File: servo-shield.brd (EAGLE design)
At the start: 65 x 56 mm, 30 parts, among them IC1 24AA01P, K1 PIN20X2

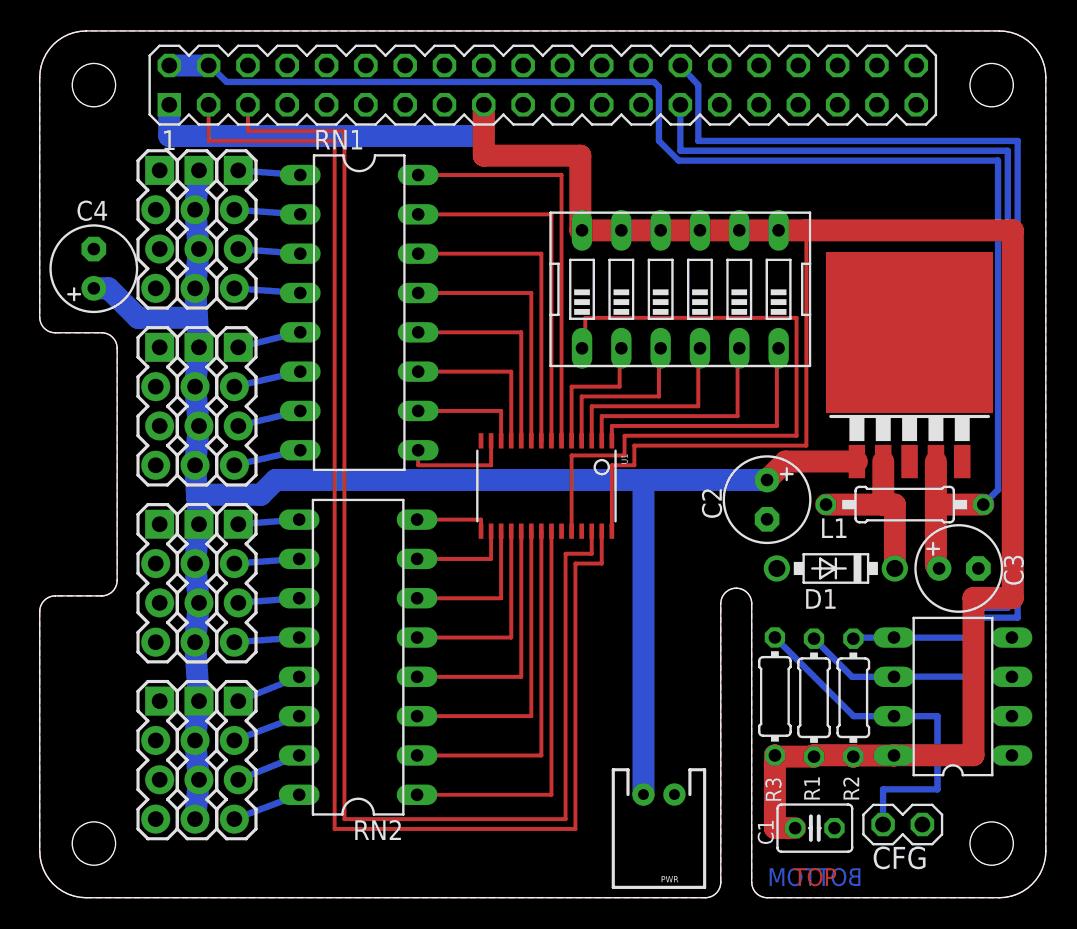
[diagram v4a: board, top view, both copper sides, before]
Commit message: Fix DRC errors. Wish I'd done that before ordering the blasted boards
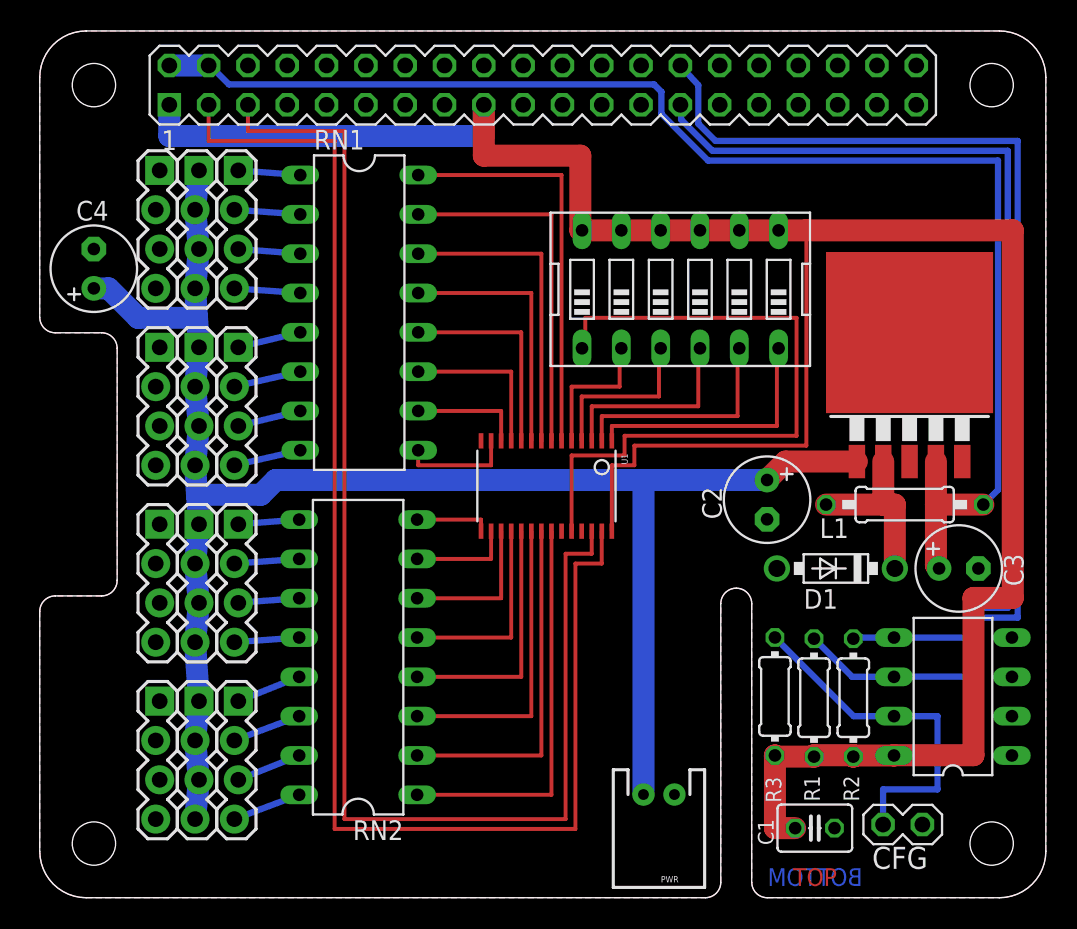
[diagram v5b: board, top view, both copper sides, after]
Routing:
- net ID_SDA: track 65.6 -> 64.4 mm
- net +5V: track 90.8 -> 89.6 mm
- net ID_SCL: track 74.8 -> 74.1 mm
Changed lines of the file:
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@@
 <?xml version="1.0" encoding="utf-8"?>
 <!DOCTYPE eagle SYSTEM "eagle.dtd">
-<eagle version="6.5.0">
+<eagle version="7.0.0">
 <drawing>
 <settings>
@@
 <setting verticaltext="up"/>
 </settings>
-<grid distance="0.0125" unitdist="inch" unit="inch" style="lines" multiple="1" display="yes" altdistance="0.025" altunitdist="inch" altunit="inch"/>
+<grid distance="0.00625" unitdist="inch" unit="inch" style="dots" multiple="1" display="yes" altdistance="0.025" altunitdist="inch" altunit="inch"/>
 <layers>
 <layer number="1" name="Top" color="4" fill="1" visible="yes" active="yes"/>
@@
 </class>
 </classes>
-<designrules name="ITEADstudio_DRC">
+<designrules name="LaenPCBOrder">
 <description language="de">&lt;b&gt;EAGLE Design Rules&lt;/b&gt;
 &lt;p&gt;
@@
 Einstellungen hier und speichern die Design Rules unter
 einem neuen Namen ab.</description>
-<description language="en">&lt;b&gt;EAGLE Design Rules&lt;/b&gt;
+<description language="en">&lt;b&gt;Laen's PCB Order Design Rules&lt;/b&gt;
 &lt;p&gt;
-The default Design Rules have been set to cover
-a wide range of applications. Your particular design
-may have different requirements, so please make the
-necessary adjustments and save your customized
-design rules under a new name.</description>
-<description language="zh">&lt;b&gt;Seeed Studio EAGLE Design Rules&lt;/b&gt;
-</description>
+Please make sure your boards conform to these design rules.</description>
 <param name="layerSetup" value="(1*16)"/>
-<param name="mtCopper" value="0.035mm 0.035mm 0.035mm 0.035mm 0.035mm 0.035mm 0.035mm 0.035mm 0.035mm 0.035mm 0.035mm 0.035mm 0.035mm 0.035mm 0.035mm 0.035mm"/>
-<param name="mtIsolate" value="1.5mm 0.15mm 0.2mm 0.15mm 0.2mm 0.15mm 0.2mm 0.15mm 0.2mm 0.15mm 0.2mm 0.15mm 0.2mm 0.15mm 0.2mm"/>
+<param name="mtCopper" value="0.0356mm 0.0356mm 0.0356mm 0.0356mm 0.0356mm 0.0356mm 0.0356mm 0.0356mm 0.0356mm 0.0356mm 0.0356mm 0.0356mm 0.0356mm 0.0356mm 0.0356mm 0.0356mm"/>
+<param name="mtIsolate" value="1.5011mm 0.1499mm 0.2007mm 0.1499mm 0.2007mm 0.1499mm 0.2007mm 0.1499mm 0.2007mm 0.1499mm 0.2007mm 0.1499mm 0.2007mm 0.1499mm 0.2007mm"/>
 <param name="mdWireWire" value="6mil"/>
 <param name="mdWirePad" value="6mil"/>
@@
 <param name="mdPadVia" value="6mil"/>
 <param name="mdViaVia" value="6mil"/>
-<param name="mdSmdPad" value="0mil"/>
-<param name="mdSmdVia" value="0mil"/>
-<param name="mdSmdSmd" value="0mil"/>
+<param name="mdSmdPad" value="6mil"/>
+<param name="mdSmdVia" value="6mil"/>
+<param name="mdSmdSmd" value="6mil"/>
 <param name="mdViaViaSameLayer" value="8mil"/>
 <param name="mnLayersViaInSmd" value="2"/>
-<param name="mdCopperDimension" value="10mil"/>
-<param name="mdDrill" value="10mil"/>
+<param name="mdCopperDimension" value="15mil"/>
+<param name="mdDrill" value="6mil"/>
 <param name="mdSmdStop" value="0mil"/>
 <param name="msWidth" value="6mil"/>
-<param name="msDrill" value="12mil"/>
-<param name="msMicroVia" value="12mil"/>
+<param name="msDrill" value="13mil"/>
+<param name="msMicroVia" value="13mil"/>
 <param name="msBlindViaRatio" value="0.5"/>
 <param name="rvPadTop" value="0.25"/>
@@
 <param name="rvMicroViaOuter" value="0.25"/>
 <param name="rvMicroViaInner" value="0.25"/>
-<param name="rlMinPadTop" value="10mil"/>
+<param name="rlMinPadTop" value="7mil"/>
 <param name="rlMaxPadTop" value="20mil"/>
-<param name="rlMinPadInner" value="10mil"/>
+<param name="rlMinPadInner" value="7mil"/>
 <param name="rlMaxPadInner" value="20mil"/>
-<param name="rlMinPadBottom" value="10mil"/>
+<param name="rlMinPadBottom" value="7mil"/>
 <param name="rlMaxPadBottom" value="20mil"/>
-<param name="rlMinViaOuter" value="6mil"/>
+<param name="rlMinViaOuter" value="7mil"/>
 <param name="rlMaxViaOuter" value="20mil"/>
-<param name="rlMinViaInner" value="6mil"/>
+<param name="rlMinViaInner" value="7mil"/>
 <param name="rlMaxViaInner" value="20mil"/>
 <param name="rlMinMicroViaOuter" value="4mil"/>
@@
 <param name="psTop" value="-1"/>
 <param name="psBottom" value="-1"/>
-<param name="psFirst" value="0"/>
+<param name="psFirst" value="-1"/>
 <param name="psElongationLong" value="100"/>
 <param name="psElongationOffset" value="100"/>
 <param name="mvStopFrame" value="1"/>
 <param name="mvCreamFrame" value="0"/>
-<param name="mlMinStopFrame" value="2mil"/>
-<param name="mlMaxStopFrame" value="2mil"/>
+<param name="mlMinStopFrame" value="3mil"/>
+<param name="mlMaxStopFrame" value="3mil"/>
 <param name="mlMinCreamFrame" value="0mil"/>
 <param name="mlMaxCreamFrame" value="0mil"/>
-<param name="mlViaStopLimit" value="100mil"/>
+<param name="mlViaStopLimit" value="0mil"/>
 <param name="srRoundness" value="0"/>
 <param name="srMinRoundness" value="0mil"/>
@@
 <param name="checkAngle" value="0"/>
 <param name="checkFont" value="1"/>
-<param name="checkRestrict" value="0"/>
+<param name="checkRestrict" value="1"/>
 <param name="useDiameter" value="13"/>
 <param name="maxErrors" value="50"/>
@@
 <pass name="Default">
 <param name="RoutingGrid" value="50mil"/>
+<param name="AutoGrid" value="1"/>
+<param name="Efforts" value="0"/>
+<param name="TopRouterVariant" value="1"/>
 <param name="tpViaShape" value="round"/>
 <param name="PrefDir.1" value="|"/>
@@
 <wire x1="57.8993" y1="21.4757" x2="58.1025" y2="21.2725" width="1.4224" layer="1"/>
 <wire x1="10.91" y1="53.77" x2="11" y2="53.77" width="0.4064" layer="16"/>
-<wire x1="11" y1="53.77" x2="12.065" y2="52.705" width="0.4064" layer="16"/>
-<wire x1="12.065" y1="52.705" x2="39.6875" y2="52.705" width="0.4064" layer="16"/>
-<wire x1="39.6875" y1="52.705" x2="40.005" y2="52.3875" width="0.4064" layer="16"/>
-<wire x1="40.005" y1="52.3875" x2="40.005" y2="48.895" width="0.4064" layer="16"/>
-<wire x1="40.005" y1="48.895" x2="41.275" y2="47.625" width="0.4064" layer="16"/>
-<wire x1="41.275" y1="47.625" x2="61.9125" y2="47.625" width="0.4064" layer="16"/>
+<wire x1="11" y1="53.77" x2="12.22375" y2="52.54625" width="0.4064" layer="16"/>
+<wire x1="12.22375" y1="52.54625" x2="39.6875" y2="52.54625" width="0.4064" layer="16"/>
+<wire x1="39.6875" y1="52.54625" x2="40.16375" y2="52.07" width="0.4064" layer="16"/>
+<wire x1="40.16375" y1="52.07" x2="40.16375" y2="50.64125" width="0.4064" layer="16"/>
+<wire x1="40.16375" y1="50.64125" x2="43.18" y2="47.625" width="0.4064" layer="16"/>
+<wire x1="43.18" y1="47.625" x2="61.9125" y2="47.625" width="0.4064" layer="16"/>
 <wire x1="61.9125" y1="47.625" x2="61.9125" y2="26.3525" width="0.4064" layer="16"/>
 <wire x1="61.9125" y1="26.3525" x2="60.96" y2="25.4" width="0.4064" layer="16"/>
@@
 <wire x1="52.4875" y1="14.27" x2="50.0225" y2="16.735" width="0.4064" layer="16"/>
 <wire x1="41.39" y1="53.77" x2="42.545" y2="52.5" width="0.4064" layer="16"/>
-<wire x1="42.545" y1="52.5" x2="42.545" y2="48.895" width="0.4064" layer="16"/>
-<wire x1="42.545" y1="48.895" x2="63.1825" y2="48.895" width="0.4064" layer="16"/>
+<wire x1="42.545" y1="52.5" x2="42.545" y2="50.00625" width="0.4064" layer="16"/>
+<wire x1="42.545" y1="50.00625" x2="43.65625" y2="48.895" width="0.4064" layer="16"/>
+<wire x1="43.65625" y1="48.895" x2="63.1825" y2="48.895" width="0.4064" layer="16"/>
 <wire x1="63.1825" y1="48.895" x2="63.1825" y2="18.0975" width="0.4064" layer="16"/>
 <wire x1="63.1825" y1="18.0975" x2="60.6425" y2="18.0975" width="0.4064" layer="16"/>
@@
 <wire x1="55.19" y1="16.81" x2="52.6375" y2="16.81" width="0.4064" layer="16"/>
 <wire x1="52.6375" y1="16.81" x2="52.5625" y2="16.735" width="0.4064" layer="16"/>
-<wire x1="41.39" y1="51.23" x2="41.39" y2="48.26" width="0.4064" layer="16"/>
-<wire x1="41.39" y1="48.26" x2="62.5475" y2="48.26" width="0.4064" layer="16"/>
+<wire x1="41.39" y1="51.23" x2="41.43375" y2="51.1175" width="0.4064" layer="16"/>
+<wire x1="41.43375" y1="51.1175" x2="41.43375" y2="50.28" width="0.4064" layer="16"/>
+<wire x1="41.43375" y1="50.28" x2="43.45375" y2="48.26" width="0.4064" layer="16"/>
+<wire x1="43.45375" y1="48.26" x2="62.5475" y2="48.26" width="0.4064" layer="16"/>
 <wire x1="62.5475" y1="48.26" x2="62.5475" y2="18.7325" width="0.4064" layer="16"/>
 <wire x1="62.5475" y1="18.7325" x2="60.0075" y2="18.7325" width="0.4064" layer="16"/>
